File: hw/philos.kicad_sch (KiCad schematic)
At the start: 6 parts, among them U1 8086_Min_Mode, U2 SN74LS373N, U3 SN74LS373N, U4 CD4046BEE4, U5 W27C512-45Z, U6 W27C512-45Z

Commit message: hw: connected the RAM and the eeprom
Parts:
- removed U4: CD4046BEE4, N16, symbol CD4046BEE4:CD4046BEE4
- removed U6: W27C512-45Z, 28P-DIP, symbol W27C512-45Z:W27C512-45Z
- added U4: SN74LS373N, N20, symbol SN74LS373N:SN74LS373N
- added U6: CD4093BE, N14, symbol CD4093BE:CD4093BE
- added U7: 71256SA25TPGI, 71256SA25TPGI:DIP787W47P254L3467H457Q28B, symbol 71256SA25TPGI:71256SA25TPGI
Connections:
- net GND: now also U5.14 (GND), U5.22 (*OE/VPP), U4.1 (*OC), U4.10 (GND), U6.7 (VSS), U7.14 (GND)
- net VCC: now also U5.28 (VCC), U4.20 (VCC), U6.14 (VDD), U7.28 (VCC)
- net dati0: now also U5.11 (Q0), U7.11 (I/O0)
- net dati1: now also U5.12 (Q1), U7.12 (I/O1)
- net dati2: now also U5.13 (Q2), U7.13 (I/O2)
- net dati3: now also U5.15 (Q3), U7.15 (I/O3)
- net dati4: now also U5.16 (Q4), U7.16 (I/O4)
- net dati5: now also U5.17 (Q5), U7.17 (I/O5)
- net dati6: now also U5.18 (Q6), U7.18 (I/O6)
- net dati7: now also U5.19 (Q7), U7.19 (I/O7)
- net indirizzi15: now reaches U5.1 (A15)
- net indirizzi15: now also U3.12 (5Q)
- net indirizzi0: now reaches U5.10 (A0)
- net indirizzi0: now also U2.2 (1Q), U7.10 (A0)
- net indirizzi12: now reaches U5.2 (A12)
- net indirizzi12: now also U3.19 (8Q), U7.2 (A12)
- net at U5.20 (*CE): now also U6.11 (M=*G-H)
- net indirizzi10: now reaches U5.21 (A10)
- net indirizzi10: now also U3.6 (3Q), U7.21 (A10)
- net indirizzi11: now reaches U5.23 (A11)
- net indirizzi11: now also U3.9 (4Q), U7.23 (A11)
- net indirizzi9: now reaches U5.24 (A9)
- net indirizzi9: now also U3.5 (2Q), U7.24 (A9)
- net indirizzi8: now reaches U5.25 (A8)
- net indirizzi8: now also U3.2 (1Q), U7.25 (A8)
- net indirizzi13: now reaches U5.26 (A13)
- net indirizzi13: now also U3.16 (7Q), U7.26 (A13)
- net indirizzi14: now reaches U5.27 (A14)
- net indirizzi14: now also U3.15 (6Q), U7.1 (A14)
- net indirizzi7: now reaches U5.3 (A7)
- net indirizzi7: now also U2.12 (5Q), U7.3 (A7)
- net indirizzi6: now reaches U5.4 (A6)
- net indirizzi6: now also U2.15 (6Q), U7.4 (A6)
- net indirizzi5: now reaches U5.5 (A5)
- net indirizzi5: now also U2.16 (7Q), U7.5 (A5)
- net indirizzi4: now reaches U5.6 (A4)
- net indirizzi4: now also U2.19 (8Q), U7.6 (A4)
- net indirizzi3: now reaches U5.7 (A3)
- net indirizzi3: now also U2.9 (4Q), U7.7 (A3)
- net indirizzi2: now reaches U5.8 (A2)
- net indirizzi2: now also U2.6 (3Q), U7.8 (A2)
- net indirizzi1: now reaches U5.9 (A1)
- net indirizzi1: now also U2.5 (2Q), U7.9 (A1)
- net at U1.25 (ALE), U2.11 (LE), U3.11 (LE): now also U4.11 (LE)
- net at U1.28 (M/~{IO}): now also U6.5 (C), U6.6 (D)
- net at U1.29 (~{WR}): now also U7.27 (~{WE})
- net at U1.32 (~{RD}): now also U7.22 (~{OE})
- net at U1.35 (A19/S6): now also U4.8 (4D)
- net at U1.36 (A18/S5): now also U4.7 (3D)
- net at U1.37 (A17/S4): now also U4.4 (2D)
- net at U1.38 (A16/S3): now also U4.3 (1D)
- new net: U6.10 (L=*E-F), U7.20 (~{CS})
- new net: U4.9 (4Q), U6.1 (A), U6.13 (H), U6.2 (B)
- new net: U6.12 (G), U6.4 (K=*C-D), U6.8 (E)
- new net: U6.3 (J=*A-B), U6.9 (F)
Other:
- moved on the sheet: U5

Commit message: hw: added clock
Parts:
- added C1, C2: 15pF, K150J15C0GF5TL2_VIS, symbol K150J15C0GF5TL2:K150J15C0GF5TL2
- added R1: 270 ohm, symbol Device:R
- added R2: 1M ohm, symbol Device:R
- added U8: SN74LS161AN, N16, symbol SN74LS161AN:SN74LS161AN
- added U9: SN74AHC14N, N14, symbol SN74AHC14N:SN74AHC14N
- added Y1: Crystal 15 MHz, symbol Device:Crystal
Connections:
- net GND: now also C1.2, C2.2, U8.3 (A), U8.4 (B), U8.5 (C), U8.6 (D), U8.8 (GND), U9.7 (GND)
- net VCC: now also U8.1 (*CLR), U8.10 (ENT), U8.16 (VCC), U8.7 (ENP), U8.9 (*LOAD), U9.14 (VCC)
- net at U1.19 (CLK): now also U8.14 (QA)
- new net: R1.1, R2.2, U8.2 (CLK), U9.2 (1Y)
- new net: C1.1, R1.2, Y1.2
- new net: C2.1, R2.1, U9.1 (1A), Y1.1
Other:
- moved on the sheet: U1, U2, U3, U4, U5, U6, U7

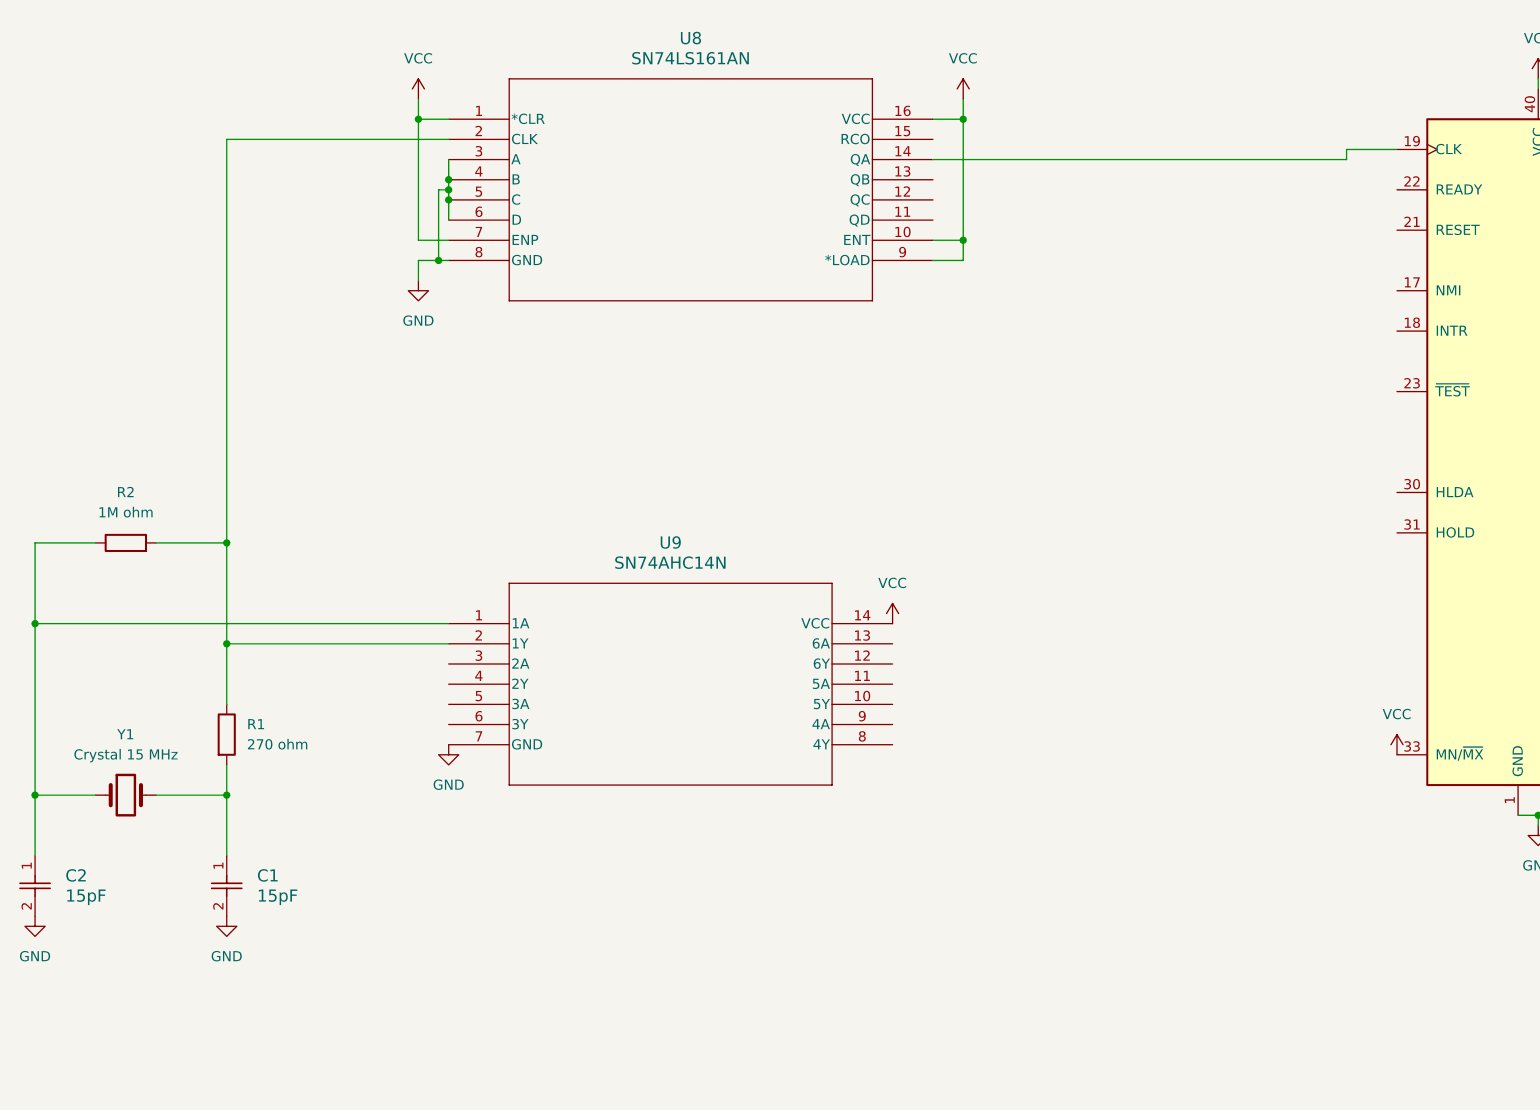
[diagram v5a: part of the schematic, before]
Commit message: hw:  added reset button
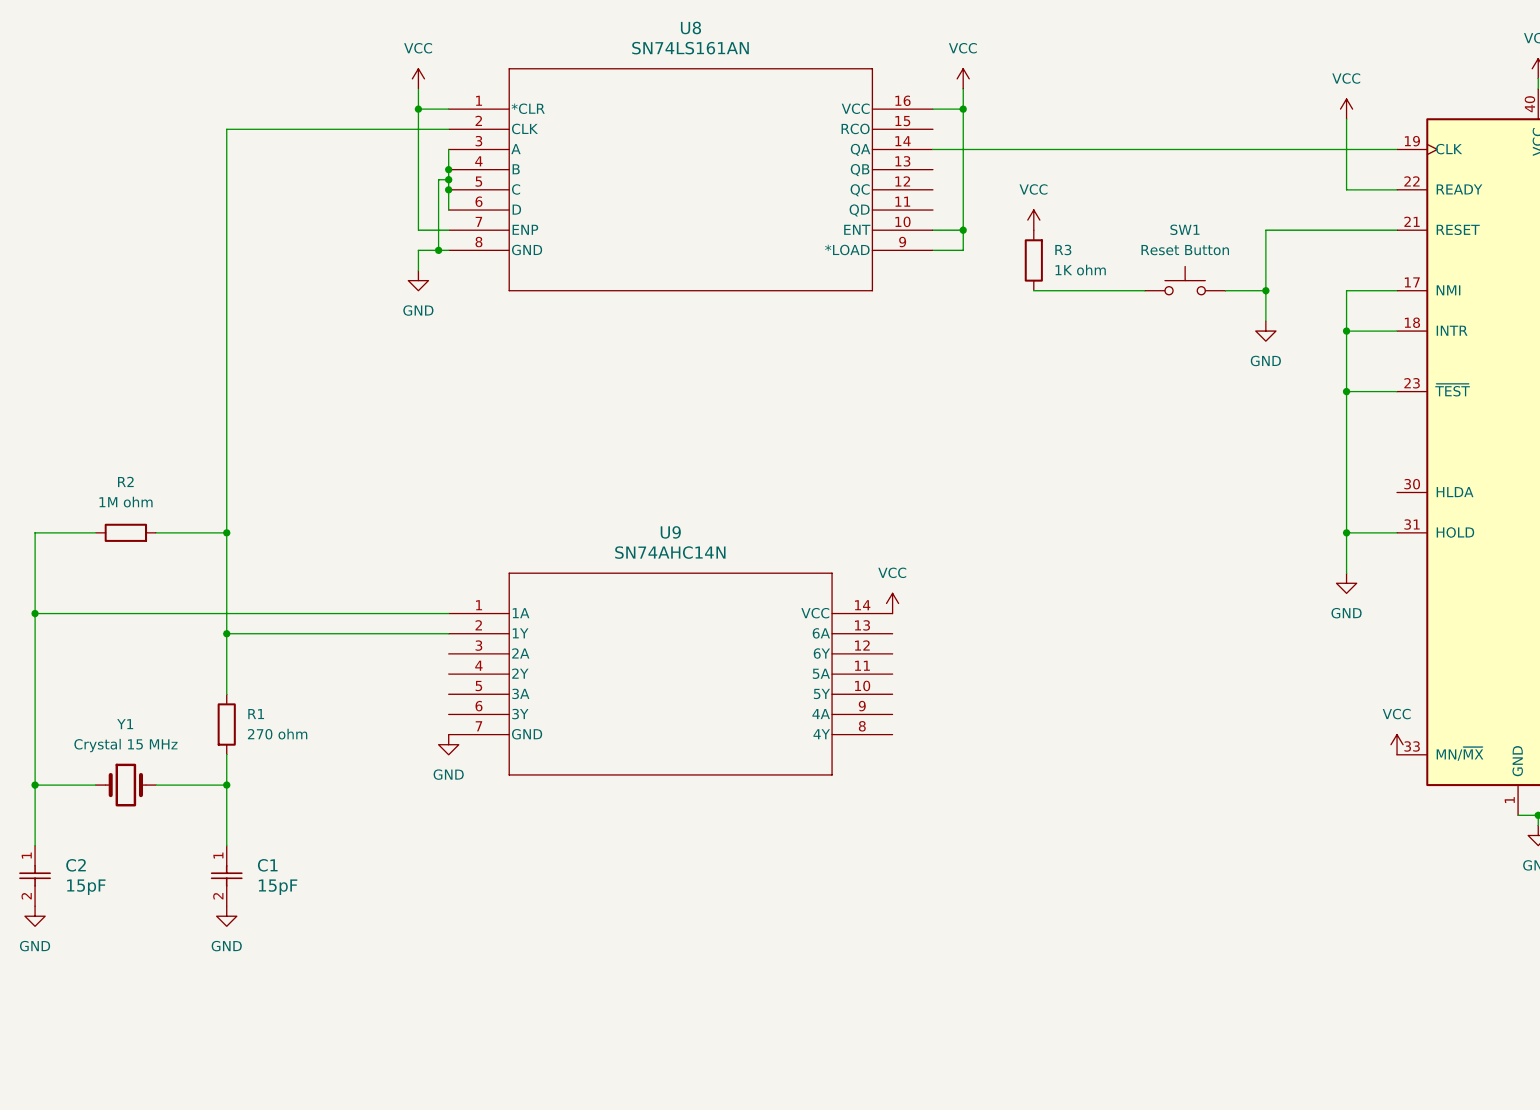
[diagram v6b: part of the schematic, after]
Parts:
- added R3: 1K ohm, symbol Device:R
- added SW1: Reset Button, symbol Switch:SW_Push
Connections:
- net GND: now also U1.17 (NMI), U1.18 (INTR), U1.21 (RESET), U1.23 (~{TEST}), U1.31 (HOLD), SW1.2
- net VCC: now also U1.22 (READY), R3.2
- new net: R3.1, SW1.1
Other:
- moved on the sheet: C1, C2, R1, R2, U8, U9, Y1

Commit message: hw: add LCD, 8251 and max232
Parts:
- removed U6: CD4093BE, N14, symbol CD4093BE:CD4093BE
- added C3, C4: 33pF, K150J15C0GF5TL2_VIS, symbol K150J15C0GF5TL2:K150J15C0GF5TL2
- added DS1: HY1602E, Display:HY1602E, symbol Display_Character:HY1602E
- added R4: 1M ohm, symbol Device:R
- added R5: 5K ohm, symbol Device:R
- added R6: 1K ohm, symbol Device:R
- added U10: MAX232N, N16, symbol MAX232N:MAX232N
- added U11: SN74LS161AN, N16, symbol SN74LS161AN:SN74LS161AN
- added U12: SN74AHC14N, N14, symbol SN74AHC14N:SN74AHC14N
- added U6: ~, symbol P8251A:P8251A
- added Y2: Crystal 5 MHz, symbol Device:Crystal
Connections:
- net GND: now also C3.2, C4.2, DS1.1 (LEDK), DS1.3 (VSS), DS1.7 (R/~{W}), U10.15 (GND), U10.2 (Vs+), U10.6 (Vs-), U11.3 (A), U11.4 (B), U11.5 (C), U11.6 (D), U11.8 (GND), U12.7 (GND), U6.17 (*CTS), U6.21 (reset), U6.22 (*DSR), U6.4 (GND)
- net VCC: now also DS1.2 (LEDA), DS1.4 (VDD), R6.1, U10.16 (VCC), U11.1 (*CLR), U11.10 (ENT), U11.16 (VCC), U11.7 (ENP), U11.9 (*LOAD), U12.14 (VCC), U6.23 (*RTS), U6.26 (Vcc)
- net dati0: now also DS1.9 (DB0), U6.27 (D0)
- net dati1: now also DS1.10 (DB1), U6.28 (D1)
- net dati2: now also DS1.11 (DB2), U6.1 (D2)
- net dati3: now also DS1.12 (DB3), U6.2 (D3)
- net dati4: now also DS1.13 (DB4), U6.5 (D4)
- net dati5: now also DS1.14 (DB5), U6.6 (D5)
- net dati6: now also DS1.15 (DB6), U6.7 (D6)
- net dati7: now also DS1.16 (DB7), U6.8 (D7)
- net at U1.32 (~{RD}), U7.22 (~{OE}): now also U6.13 (*RD)
- net at U1.29 (~{WR}), U7.27 (~{WE}): now also U6.10 (*WR)
- net indirizzi19: now reaches U4.9 (4Q)
- net indirizzi19: now also DS1.6 (RS), U6.12 (C/*D)
- net indirizzi16: now reaches U4.2 (1Q)
- net indirizzi17: now reaches U4.5 (2Q)
- net indirizzi18: now reaches U4.6 (3Q)
- new net: C4.1, R5.2, Y2.2
- new net: C3.1, R4.1, U12.1 (1A), Y2.1
- new net: R4.2, R5.1, U11.2 (CLK), U12.2 (1Y)
- new net: U10.1 (C1+), U10.3 (C1-)
- new net: U10.11 (T1IN), U6.19 (TxD)
- new net: U10.12 (R1OUT), U6.3 (RxD)
- new net: U10.4 (C2+), U10.5 (C2-)
- new net: DS1.5 (Vo), R6.2
- new net: U11.13 (QB), U6.20 (CLK)
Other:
- moved on the sheet: C1, C2, R1, R2, R3, SW1, U1, U2, U3, U4, U5, U7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

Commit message: hw: add more memory
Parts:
- removed C3, C4: 33pF, K150J15C0GF5TL2_VIS, symbol K150J15C0GF5TL2:K150J15C0GF5TL2
- removed R4: 1M ohm, symbol Device:R
- removed R5: 5K ohm, symbol Device:R
- removed U11: SN74LS161AN, N16, symbol SN74LS161AN:SN74LS161AN
- removed U12: SN74AHC14N, N14, symbol SN74AHC14N:SN74AHC14N
- removed Y2: Crystal 5 MHz, symbol Device:Crystal
- added U11: W27C512-45Z, 28P-DIP, symbol W27C512-45Z:W27C512-45Z
- added U12: 71256SA25TPGI, 71256SA25TPGI:DIP787W47P254L3467H457Q28B, symbol 71256SA25TPGI:71256SA25TPGI
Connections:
- net GND: now also U11.14 (GND), U11.22 (*OE/VPP), U12.14 (GND)
- net VCC: now also U11.28 (VCC), U12.28 (VCC)
- net dati0: now also U11.11 (Q0)
- net dati1: now also U11.12 (Q1)
- net dati10: now also U12.13 (I/O2)
- net dati11: now also U12.15 (I/O3)
- net dati12: now also U12.16 (I/O4)
- net dati13: now also U12.17 (I/O5)
- net dati14: now also U12.18 (I/O6)
- net dati15: now also U12.19 (I/O7)
- net dati2: now also U11.13 (Q2)
- net dati3: now also U11.15 (Q3)
- net dati4: now also U11.16 (Q4)
- net dati5: now also U11.17 (Q5)
- net dati6: now also U11.18 (Q6)
- net dati7: now also U11.19 (Q7)
- net dati8: now also U12.11 (I/O0)
- net dati9: now also U12.12 (I/O1)
- net indirizzi0: now also U11.10 (A0), U12.10 (A0)
- net indirizzi1: now also U11.9 (A1), U12.9 (A1)
- net indirizzi10: now also U11.21 (A10), U12.21 (A10)
- net indirizzi11: now also U11.23 (A11), U12.23 (A11)
- net indirizzi12: now also U11.2 (A12), U12.2 (A12)
- net indirizzi13: now also U11.26 (A13), U12.26 (A13)
- net indirizzi14: now also U11.27 (A14), U12.1 (A14)
- net indirizzi15: now also U11.1 (A15)
- net indirizzi2: now also U11.8 (A2), U12.8 (A2)
- net indirizzi3: now also U11.7 (A3), U12.7 (A3)
- net indirizzi4: now also U11.6 (A4), U12.6 (A4)
- net indirizzi5: now also U11.5 (A5), U12.5 (A5)
- net indirizzi6: now also U11.4 (A6), U12.4 (A6)
- net indirizzi7: now also U11.3 (A7), U12.3 (A7)
- net indirizzi8: now also U11.25 (A8), U12.25 (A8)
- net indirizzi9: now also U11.24 (A9), U12.24 (A9)
- net at U8.11 (QD): now also U6.20 (CLK)
- net at U1.32 (~{RD}), U6.13 (*RD), U7.22 (~{OE}): now also U12.22 (~{OE})
- net at U1.29 (~{WR}), U6.10 (*WR), U7.27 (~{WE}): now also U12.27 (~{WE})
